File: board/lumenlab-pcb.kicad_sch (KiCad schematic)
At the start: 26 parts, among them J1 2.1mm Barrel Jack, SW1 SW_SPST, U1 MP2338, U2 AP7361C-33E, U3 ESP32-WROOM-32D

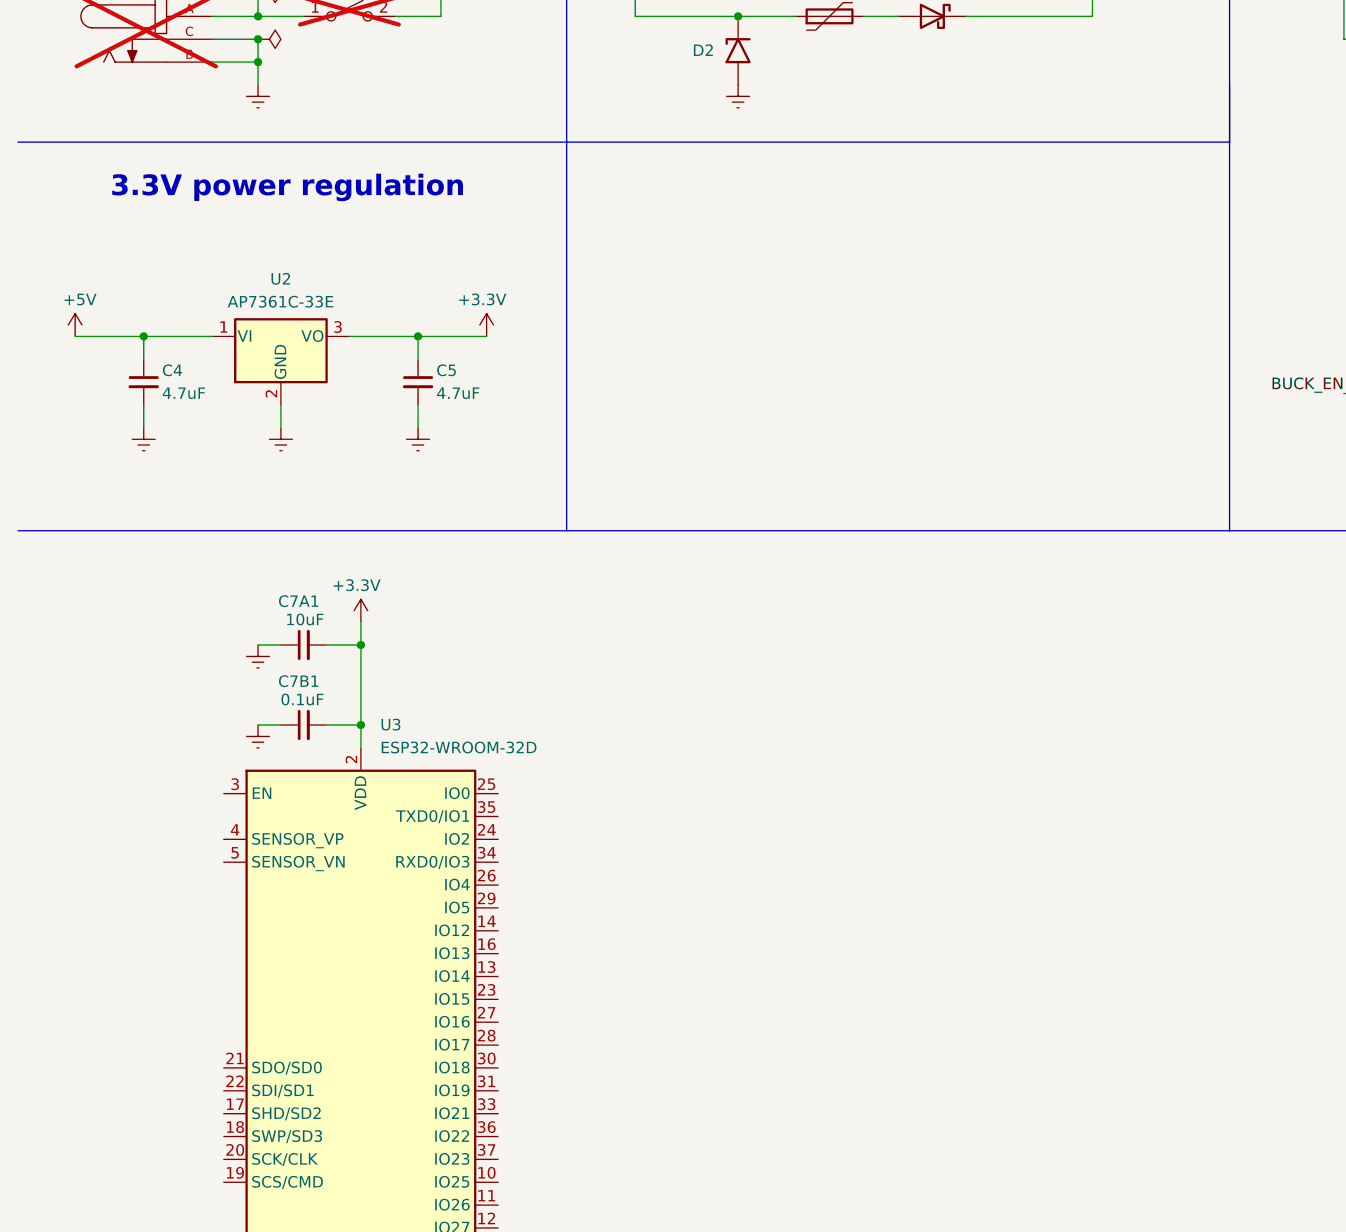
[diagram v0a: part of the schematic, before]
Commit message: Wire logic level shifter with docs
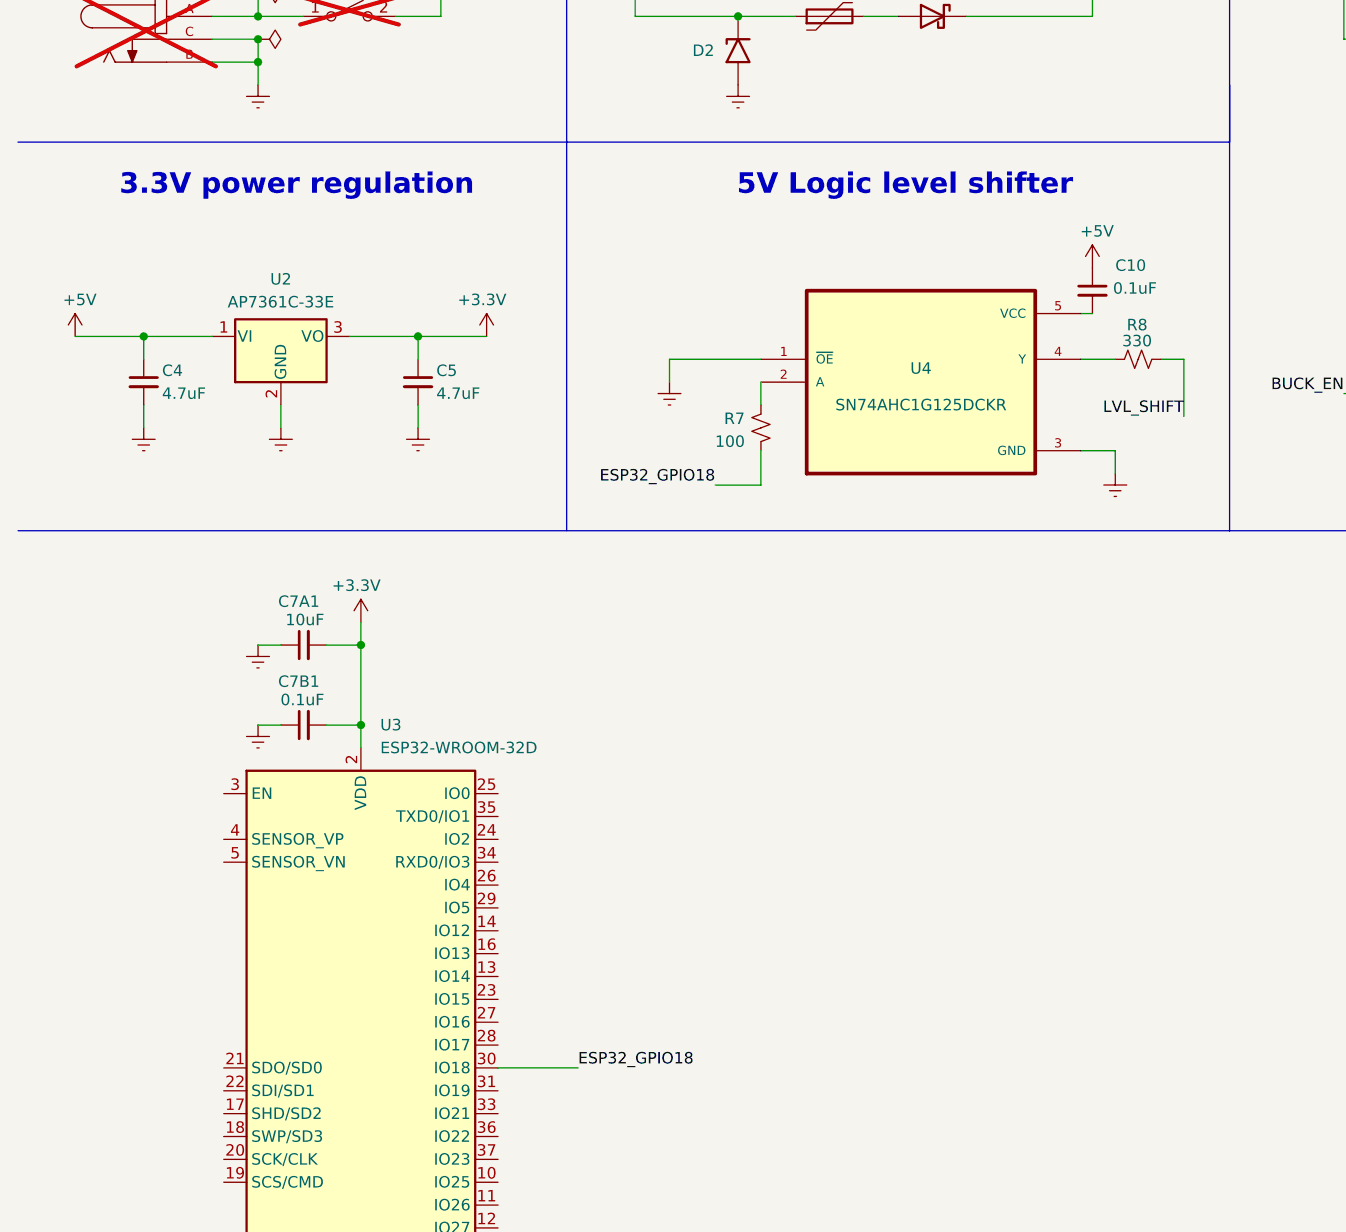
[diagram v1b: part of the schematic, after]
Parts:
- added C10: 0.1uF, Capacitor_SMD:C_1210_3225Metric_Pad1.33x2.70mm_HandSolder, symbol Device:C_Small
- added R7: 100, Resistor_SMD:R_0603_1608Metric_Pad0.98x0.95mm_HandSolder, symbol Device:R_Small_US
- added R8: 330, Resistor_SMD:R_0603_1608Metric_Pad0.98x0.95mm_HandSolder, symbol Device:R_Small_US
- added U4: SN74AHC1G125DCKR, SN74AHC1G125DCKR:SOT65P210X110-5N, symbol 1_Custom_SN74AHC1G125DCKR:SN74AHC1G125DCKR
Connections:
- net +5V: now also C10.1
- net GND: now also U4.1 (~{OE}), U4.3 (GND)
- net ESP32_GPIO18: now reaches U3.30 (IO18)
- net ESP32_GPIO18: now also R7.2
- new net: C10.2, U4.5 (VCC)
- new net: R7.1, U4.2 (A)
- new net: R8.2, U4.4 (Y)
- new net LVL_SHIFT: R8.1
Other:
- note added: "5V Logic level shifter"

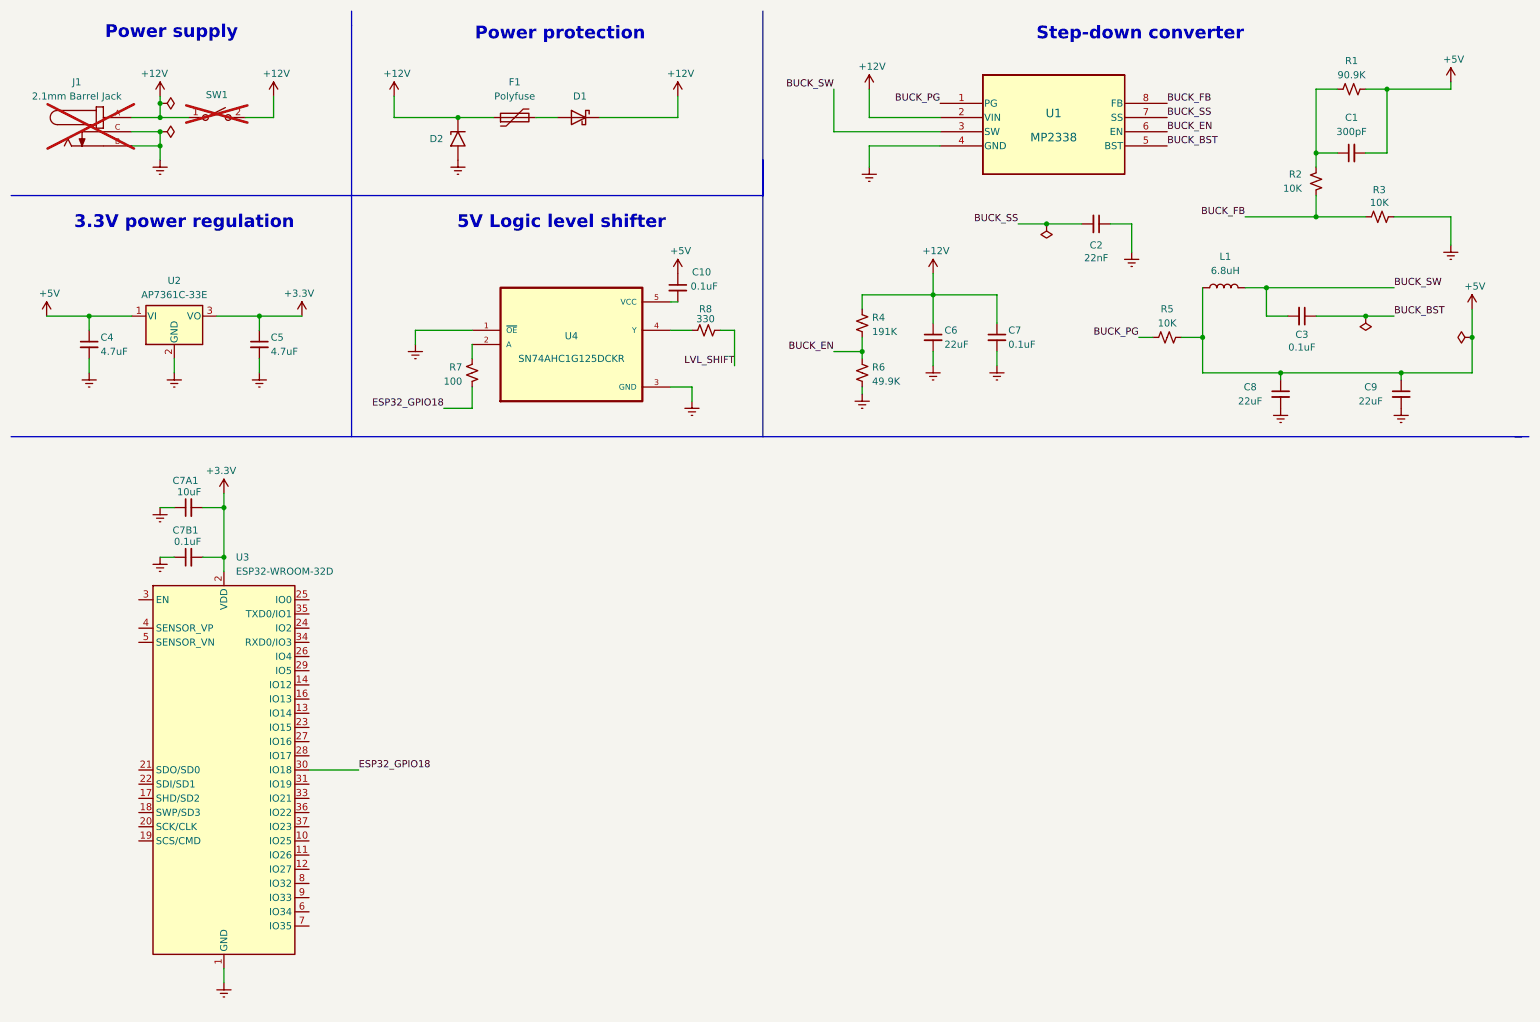
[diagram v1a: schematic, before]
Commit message: Exchange quad with single gate logic-level shifter
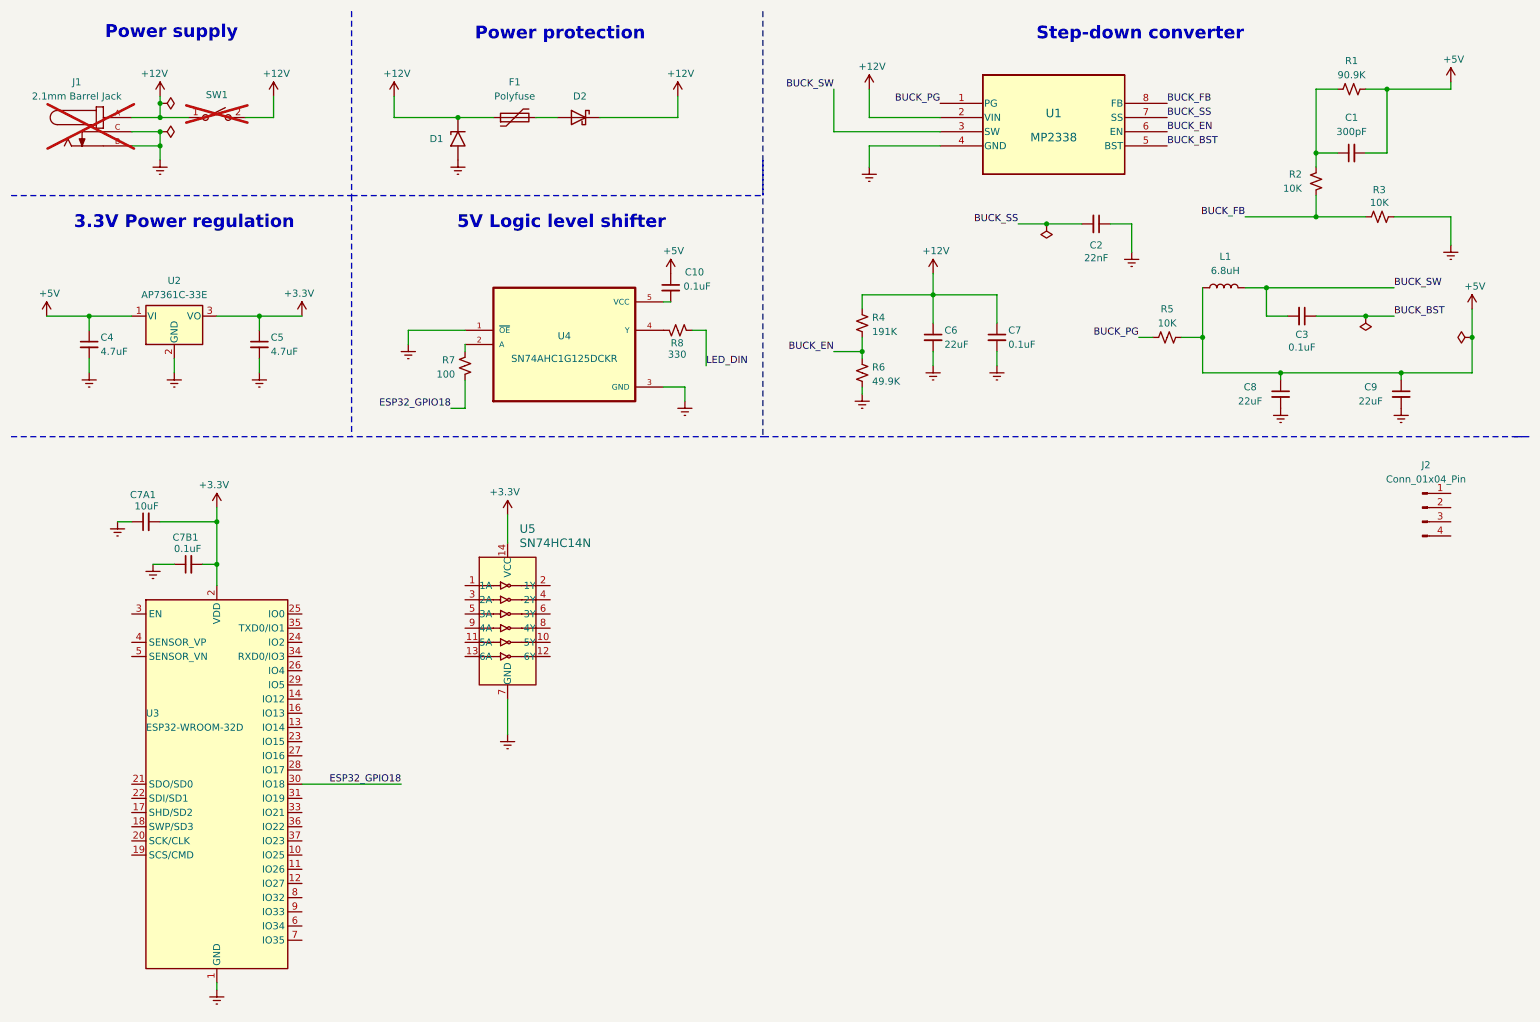
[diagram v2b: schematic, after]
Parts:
- added J2: Conn_01x04_Pin, Connector_JST:JST_EH_S4B-EH_1x04_P2.50mm_Horizontal, symbol Connector:Conn_01x04_Pin
- added U5: SN74HC14N, digikey-footprints:DIP-14_W3mm, symbol dk_Logic-Gates-and-Inverters:SN74HC14N
- renumbered D2 to D1, D1 to D2
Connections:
- net +3.3V: now also U5.14 (VCC)
- net GND: now also U5.7 (GND)
- net LVL_SHIFT renamed LED_DIN
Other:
- note added: "3.3V Power regulation"
- note removed: "3.3V power regulation"
- moved on the sheet: C10, C7A1, C7B1, R7, R8, U3, U4

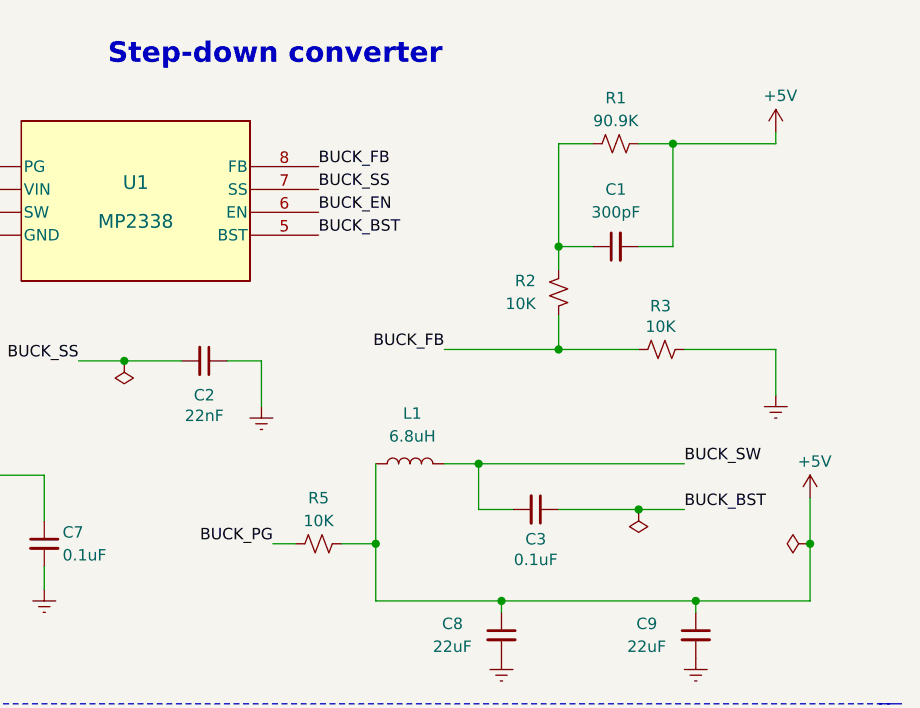
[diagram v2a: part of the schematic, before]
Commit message: Fix series feedback resistor in schematic
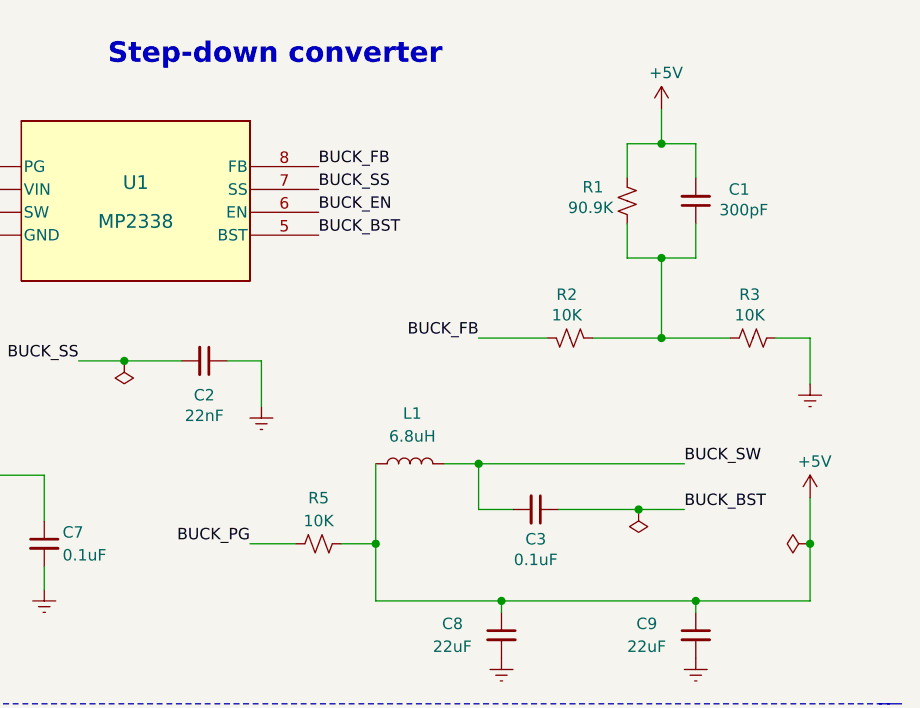
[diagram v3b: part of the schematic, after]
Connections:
- net BUCK_FB: no longer R3.1
- net at C1.1, R1.1, R2.1: now also R3.1
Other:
- moved on the sheet: C1, R1, R2, R3
